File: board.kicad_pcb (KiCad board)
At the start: 4 copper layers, 72 x 46.5 mm, 49 parts, among them J1 H3, J2 USB-UART, J3 H2, J4 H1, J5 PWR, J6 DL, J7 H4, Q1 Q_NPN_BCE, Q2 Q_NPN_BCE, SW1 RESET, U1 ASSoC, U2 LM1117-3.3, U3 LM1117-3.3, Y1 25 MHz

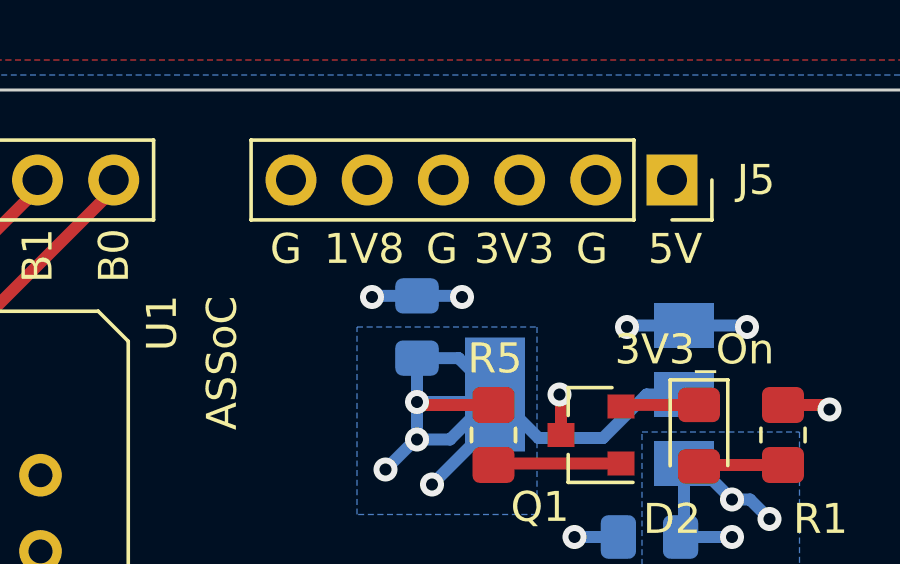
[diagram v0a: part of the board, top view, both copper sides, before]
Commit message: Remove 3Ds, fix 3V3 and 1V8 switched labels
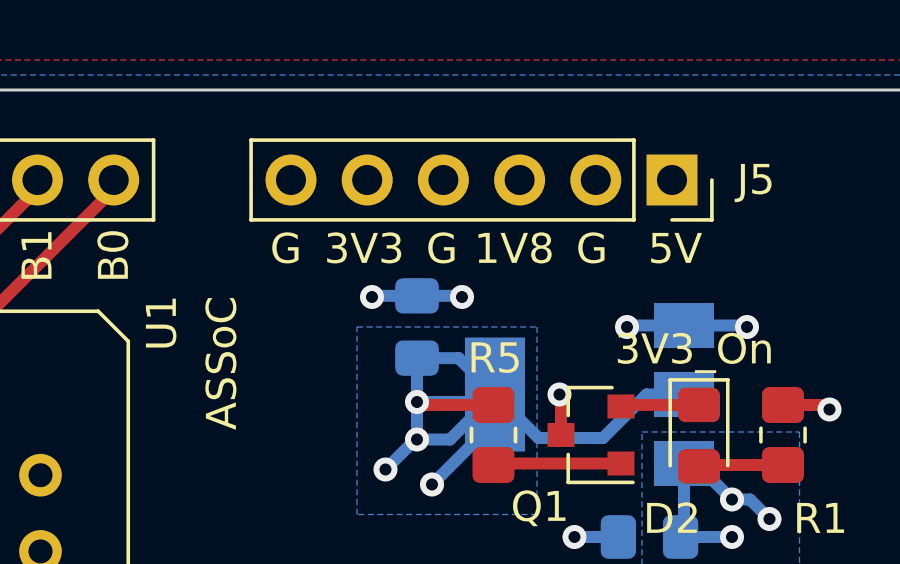
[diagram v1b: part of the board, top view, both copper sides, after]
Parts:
- removed G***: LOGO, GAPH-Extra:Astaroth-Seal
- C18: value 18n -> 18p
- U2: value LM1117-3.3 -> LM1117-1.8

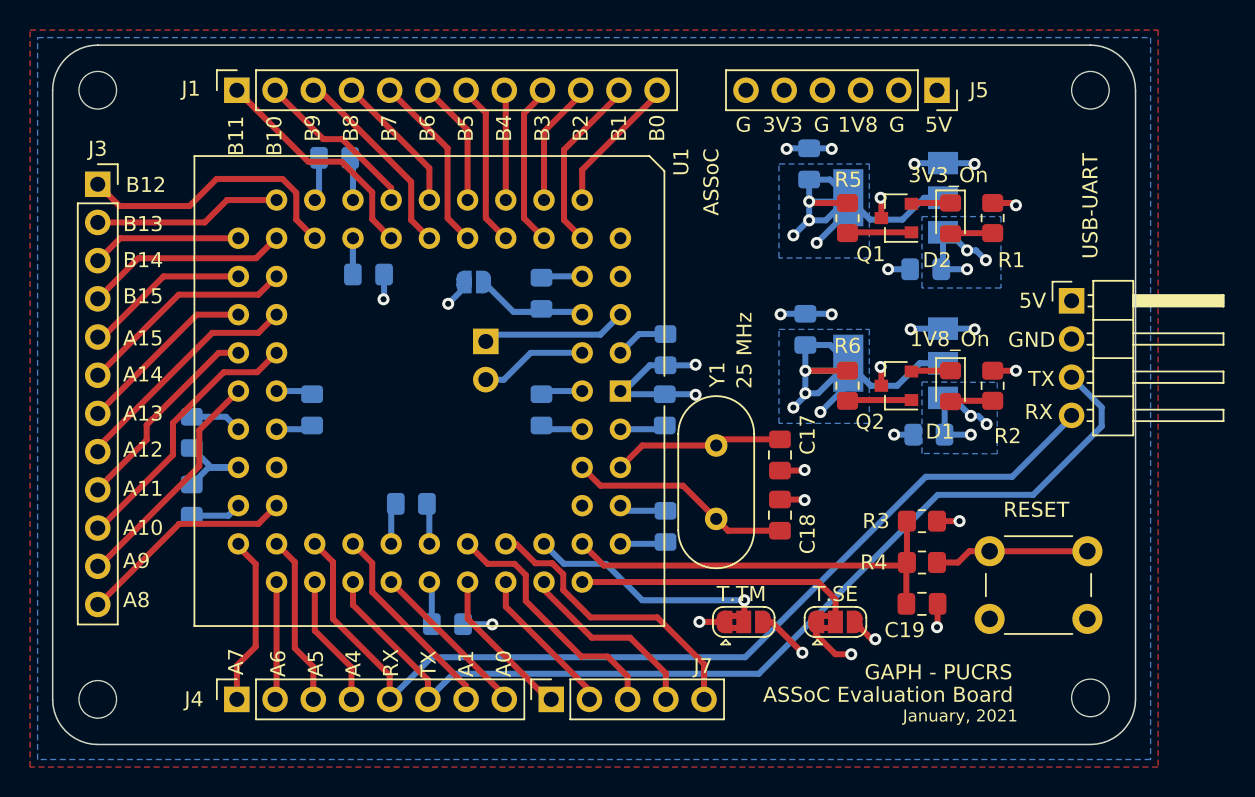
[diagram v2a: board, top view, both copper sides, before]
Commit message: Convert project to Kicad v6
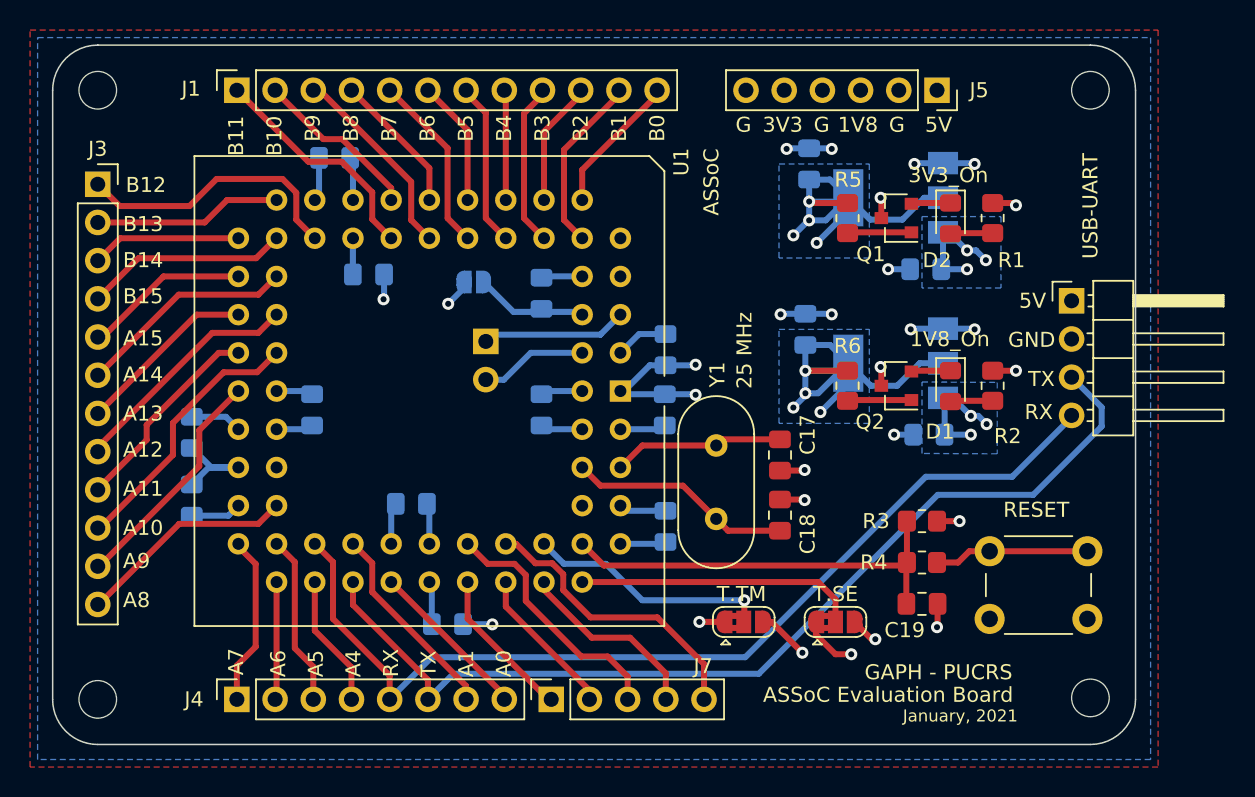
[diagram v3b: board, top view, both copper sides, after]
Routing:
- added copper zone on In2.Cu, net +1V8
- added copper zone on In2.Cu, net +3V3
- added copper zone on In2.Cu, net +5V
- added copper zone on In1.Cu, net GND
- removed copper zone on Pwr, net +1V8
- removed copper zone on Pwr, net +3V3
- removed copper zone on Pwr, net +5V
- removed copper zone on Gnd, net GND
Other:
- net class Default removed
